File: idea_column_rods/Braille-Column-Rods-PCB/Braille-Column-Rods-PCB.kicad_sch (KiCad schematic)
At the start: 6 parts, among them J1 Conn_01x03, J5 Screw_Terminal_01x02, J6 Screw_Terminal_01x02

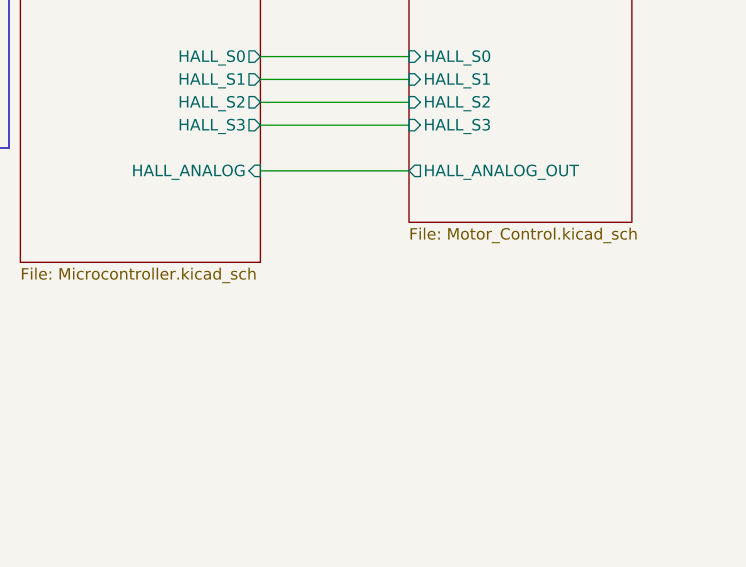
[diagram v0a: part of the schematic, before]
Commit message: WIP: Rods PCB placement
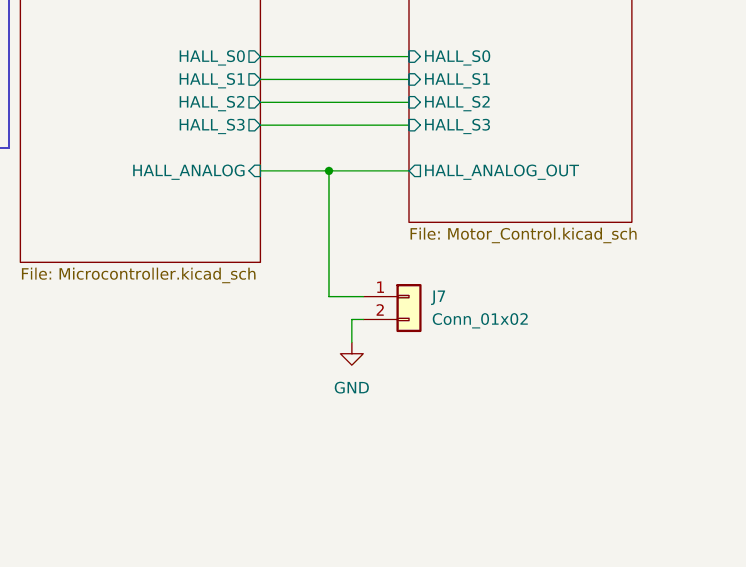
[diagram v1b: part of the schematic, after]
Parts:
- added J7: Conn_01x02, Connector_PinHeader_2.54mm:PinHeader_1x02_P2.54mm_Vertical, symbol Connector_Generic:Conn_01x02
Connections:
- net GND: now also J7.2 (Pin_2)
- net Microcontroller/HALL_ANALOG: now also J7.1 (Pin_1)
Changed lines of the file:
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@@
 	(generator_version "8.0")
 	(paper "USLetter")
+	(junction
+		(at 99.06 71.12)
+		(diameter 0)
+		(color 0 0 0 0)
+	)
 	(wire
 		(pts
@@
 	(wire
 		(pts
-			(xy 91.44 71.12) (xy 107.95 71.12)
+			(xy 91.44 71.12) (xy 99.06 71.12)
+		)
+		(stroke
+			(width 0)
+			(type default)
+		)
+	)
+	(wire
+		(pts
+			(xy 99.06 85.09) (xy 99.06 71.12)
 		)
 		(stroke
@@
 	(wire
 		(pts
+			(xy 101.6 87.63) (xy 102.87 87.63)
+		)
+		(stroke
+			(width 0)
+			(type default)
+		)
+	)
+	(wire
+		(pts
 			(xy 22.86 85.09) (xy 22.86 87.63)
 		)
@@
 	(wire
 		(pts
+			(xy 102.87 85.09) (xy 99.06 85.09)
+		)
+		(stroke
+			(width 0)
+			(type default)
+		)
+	)
+	(wire
+		(pts
 			(xy 33.02 58.42) (xy 33.02 60.96)
 		)
@@
 	(wire
 		(pts
+			(xy 99.06 71.12) (xy 107.95 71.12)
+		)
+		(stroke
+			(width 0)
+			(type default)
+		)
+	)
+	(wire
+		(pts
 			(xy 39.37 144.78) (xy 39.37 149.86)
 		)
@@
 		(pts
 			(xy 91.44 26.67) (xy 107.95 26.67)
+		)
+		(stroke
+			(width 0)
+			(type default)
+		)
+	)
+	(wire
+		(pts
+			(xy 101.6 90.17) (xy 101.6 87.63)
 		)
 		(stroke
@@
 	)
 	(symbol
+		(lib_id "Connector_Generic:Conn_01x02")
+		(at 107.95 85.09 0)
+		(unit 1)
+		(exclude_from_sim no)
+		(in_bom yes)
+		(on_board yes)
+		(dnp no)
+		(fields_autoplaced yes)
+		(property "Reference" "J7"
+			(at 110.49 85.0899 0)
+			(effects
+				(font
+					(size 1.27 1.27)
+				)
+				(justify left)
+			)
+		)
+		(property "Value" "Conn_01x02"
+			(at 110.49 87.6299 0)
+			(effects
+				(font
+					(size 1.27 1.27)
+				)
+				(justify left)
+			)
+		)
+		(property "Footprint" "Connector_PinHeader_2.54mm:PinHeader_1x02_P2.54mm_Vertical"
+			(at 107.95 85.09 0)
+			(effects
+				(font
+					(size 1.27 1.27)
+				)
+				(hide yes)
+			)
+		)
+		(property "Datasheet" "~"
+			(at 107.95 85.09 0)
+			(effects
+				(font
+					(size 1.27 1.27)
+				)
+				(hide yes)
+			)
+		)
+		(property "Description" "Generic connector, single row, 01x02, script generated (kicad-library-utils/schlib/autogen/connector/)"
+			(at 107.95 85.09 0)
+			(effects
+				(font
+					(size 1.27 1.27)
+				)
+				(hide yes)
+			)
+		)
+		(pin "2"
+		)
+		(pin "1"
+		)
+		(instances
+			(project ""
+				(path "/f7fdfeea-4cd4-4338-ad68-f9089a17ed6f"
+					(reference "J7")
+					(unit 1)
+				)
+			)
+		)
+	)
+	(symbol
 		(lib_id "power:Vdrive")
 		(at 33.02 48.26 0)
@@
 					(unit 1)
 				)
+			)
+		)
+	)
+	(symbol
+		(lib_id "power:GND")
+		(at 101.6 90.17 0)
+		(unit 1)
+		(exclude_from_sim no)
+		(in_bom yes)
+		(on_board yes)
+		(dnp no)
+		(fields_autoplaced yes)
+		(property "Reference" "#PWR0171"
+			(at 101.6 96.52 0)
+			(effects
+				(font
+					(size 1.27 1.27)
+				)
+				(hide yes)
+			)
+		)
+		(property "Value" "GND"
+			(at 101.6 95.25 0)
+			(effects
+				(font
+					(size 1.27 1.27)
+				)
+			)
+		)
+		(property "Footprint" ""
+			(at 101.6 90.17 0)
+			(effects
+				(font
+					(size 1.27 1.27)
+				)
+				(hide yes)
+			)
+		)
+		(property "Datasheet" ""
+			(at 101.6 90.17 0)
+			(effects
+				(font
+					(size 1.27 1.27)
+				)
+				(hide yes)
+			)
+		)
+		(property "Description" "Power symbol creates a global label with name \"GND\" , ground"
+			(at 101.6 90.17 0)
+			(effects
+				(font
+					(size 1.27 1.27)
+				)
+				(hide yes)
+			)
+		)
+		(pin "1"
+		)
+		(instances
+			(project ""
+				(path "/f7fdfeea-4cd4-4338-ad68-f9089a17ed6f"
+					(reference "#PWR0171")
+					(unit 1)
+				)

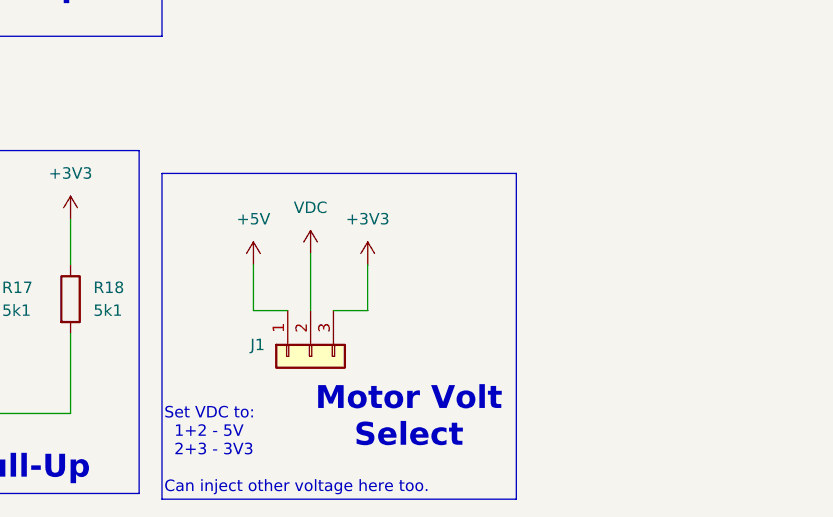
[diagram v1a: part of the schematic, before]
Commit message: WIP: Place the housing and motor X
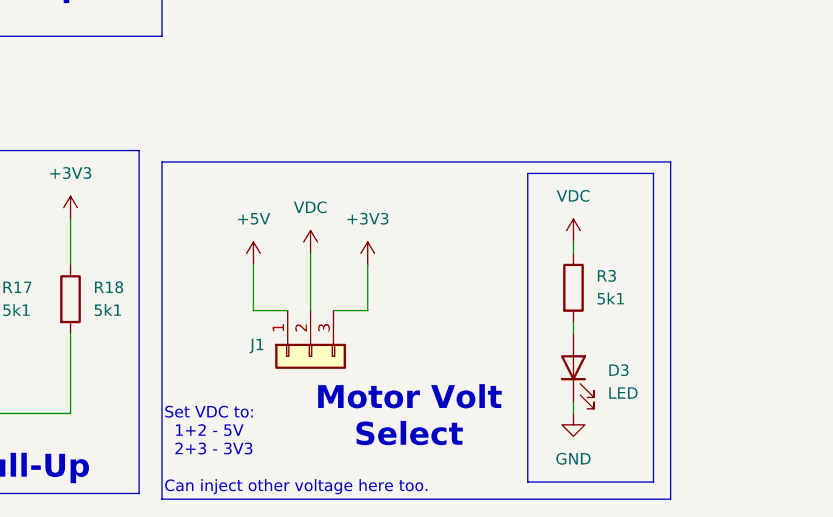
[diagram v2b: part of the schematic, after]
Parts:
- added D3: LED, LED_SMD:LED_0603_1608Metric_Pad1.05x0.95mm_HandSolder, symbol Device:LED
- added R3: 5k1, Resistor_SMD:R_0603_1608Metric_Pad0.98x0.95mm_HandSolder, symbol Device:R
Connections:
- net GND: now also D3.1 (K)
- net VDC: now also R3.1
- new net: D3.2 (A), R3.2

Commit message: WIP: Manual routing and silkscreens
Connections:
- net Vdrive is gone; now on net VDC: C9.1
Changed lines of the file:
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@@
+	(symbol
+		(lib_id "power:VDC")
+		(at 33.02 48.26 0)
+		(unit 1)
+		(exclude_from_sim no)
+		(in_bom yes)
+		(on_board yes)
+		(dnp no)
+		(property "Reference" "#PWR055"
+			(at 33.02 52.07 0)
+			(effects
+				(font
+					(size 1.27 1.27)
+				)
+				(hide yes)
+			)
+		)
+		(property "Value" "VDC"
+			(at 33.02 43.18 0)
+			(effects
+				(font
+					(size 1.27 1.27)
+				)
+			)
+		)
+		(property "Footprint" ""
+			(at 33.02 48.26 0)
+			(effects
+				(font
+					(size 1.27 1.27)
+				)
+				(hide yes)
+			)
+		)
+		(property "Datasheet" ""
+			(at 33.02 48.26 0)
+			(effects
+				(font
+					(size 1.27 1.27)
+				)
+				(hide yes)
+			)
+		)
+		(property "Description" "Power symbol creates a global label with name \"VDC\""
+			(at 33.02 48.26 0)
+			(effects
+				(font
+					(size 1.27 1.27)
+				)
+				(hide yes)
+			)
+		)
+		(pin "1"
+		)
+		(instances
+			(project "Braille-Column-Rods-PCB"
+				(path "/f7fdfeea-4cd4-4338-ad68-f9089a17ed6f"
+					(reference "#PWR055")
+					(unit 1)
+				)
+			)
+		)
+	)
 	(symbol
 		(lib_id "power:VDC")
@@
 					(unit 1)
 				)
-			)
-		)
-	)
-	(symbol
-		(lib_id "power:Vdrive")
-		(at 33.02 48.26 0)
-		(unit 1)
-		(exclude_from_sim no)
-		(in_bom yes)
-		(on_board yes)
-		(dnp no)
-		(fields_autoplaced yes)
-		(property "Reference" "#PWR055"
-			(at 33.02 52.07 0)
-			(effects
-				(font
-					(size 1.27 1.27)
-				)
-				(hide yes)
-			)
-		)
-		(property "Value" "Vdrive"
-			(at 33.02 43.18 0)
-			(effects
-				(font
-					(size 1.27 1.27)
-				)
-			)
-		)
-		(property "Footprint" ""
-			(at 33.02 48.26 0)
-			(effects
-				(font
-					(size 1.27 1.27)
-				)
-				(hide yes)
-			)
-		)
-		(property "Datasheet" ""
-			(at 33.02 48.26 0)
-			(effects
-				(font
-					(size 1.27 1.27)
-				)
-				(hide yes)
-			)
-		)
-		(property "Description" "Power symbol creates a global label with name \"Vdrive\""
-			(at 33.02 48.26 0)
-			(effects
-				(font
-					(size 1.27 1.27)
-				)
-				(hide yes)
-			)
-		)
-		(pin "1"
-		)
-		(instances
-			(project "Braille-Pogo-Frame"
-				(path "/f7fdfeea-4cd4-4338-ad68-f9089a17ed6f"
-					(reference "#PWR055")
-					(unit 1)
-				)

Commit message: Complete type 4 rev 1
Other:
- title: (none) -> Braille Cam Rod Prototype (Type 4)
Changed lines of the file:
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@@
 	(generator_version "8.0")
 	(paper "USLetter")
+	(title_block
+		(title "Braille Cam Rod Prototype (Type 4)")
+		(date "2025-01-06")
+		(rev "Rev 1")
+	)
 	(junction
 		(at 99.06 71.12)
